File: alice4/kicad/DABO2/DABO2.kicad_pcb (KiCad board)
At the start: 2 copper layers, 96 x 34.1 mm, 61 parts, among them J1 LIPO, J10 THERM, J2 LCD, J3 HOME, J4 +25mA, J5 +25mA, J6 +50mA, J7 5VOUT, J8 PWRSW, J9 5VIN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

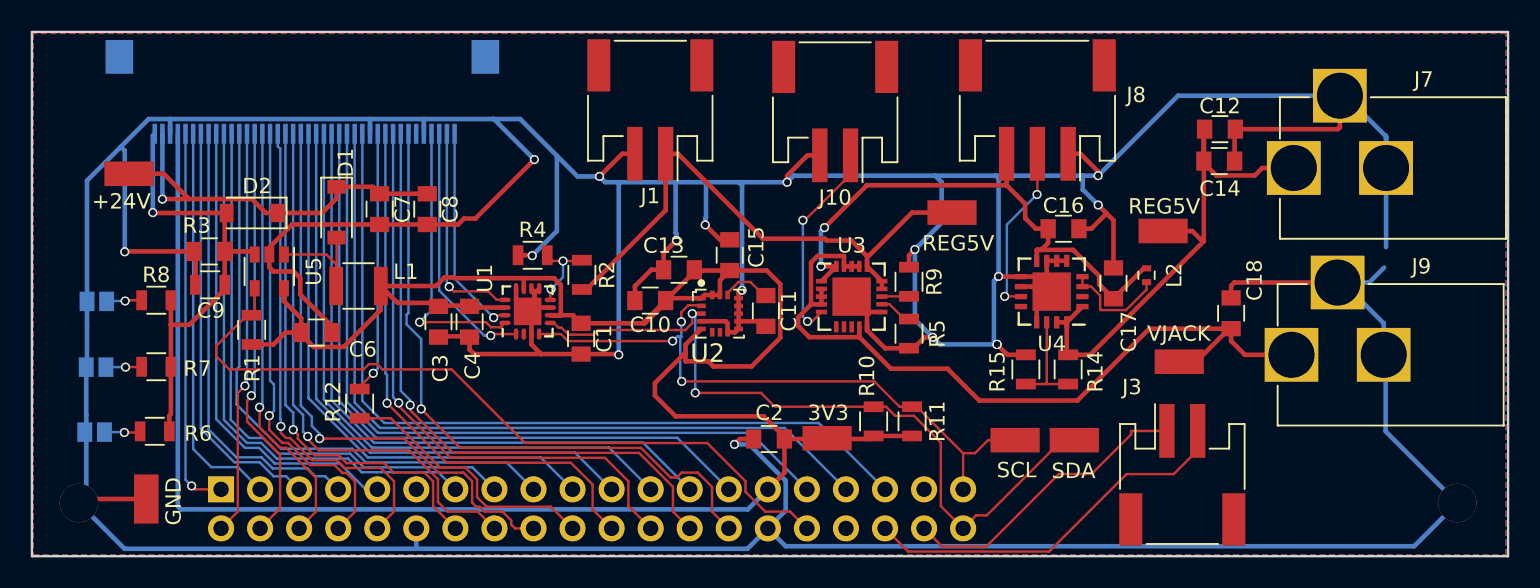
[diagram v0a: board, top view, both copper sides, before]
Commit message: fix holes, add cap for HOME
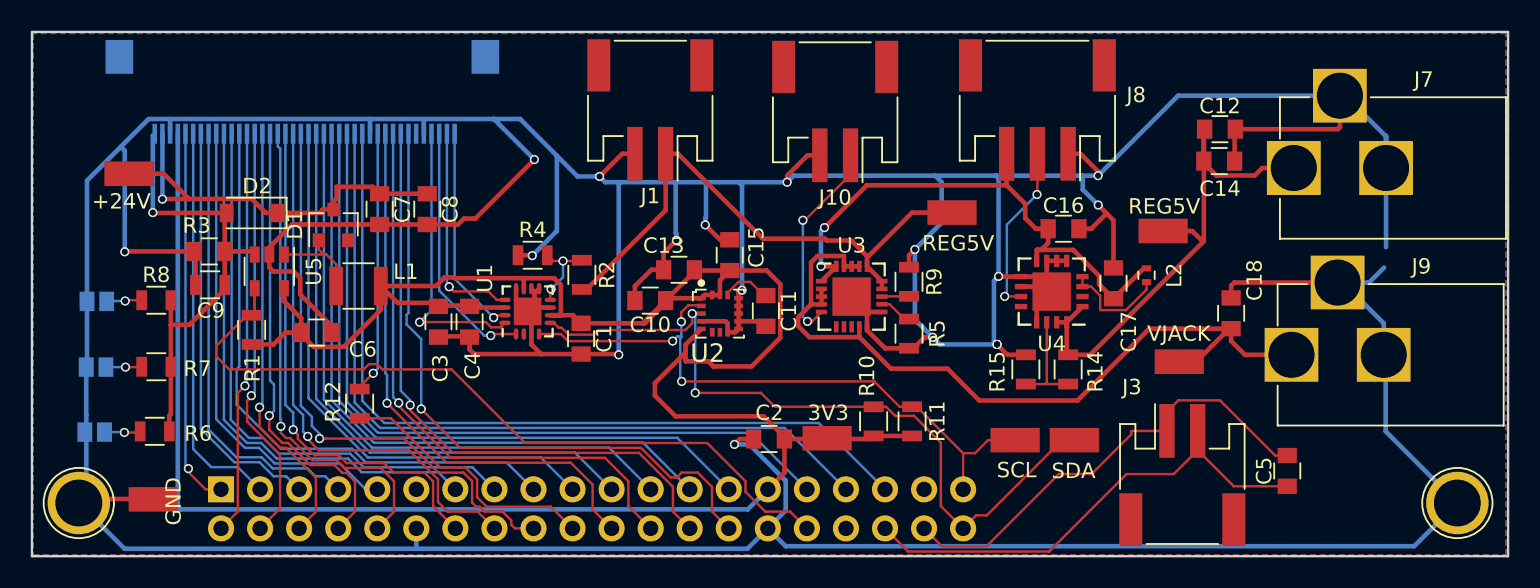
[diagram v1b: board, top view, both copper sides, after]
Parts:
- added C5: .1uF, Capacitors_SMD:C_0805, F.Cu at (186.2, 114.3)
- D1: value MBR0540 -> BAT54; footprint Diodes_SMD:D_SOD-123 -> TO_SOT_Packages_SMD:SOT-23
- HOLE0, HOLE1: footprint Mounting_Holes:MountingHole_2-5mm -> Connect:1pin
- moved D1 0.85 mm to (124.2, 98.3), turned to 90 degrees
- moved TP1 0.45 mm to (112.5, 116.1), turned to 180 degrees
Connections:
- D1 pad 1: LED-A -> Net-(D1-Pad1)
- L1 pad 2: Net-(D1-Pad2) -> Net-(D1-Pad1)
- U5 pad 1: Net-(D1-Pad2) -> Net-(D1-Pad1)
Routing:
- net HOME1: track 19.5 -> 30.4 mm
- net Net-(D1-Pad2): track 8.24 -> 0.00 mm
- net HOME0: track 24.9 -> 31.7 mm
- net Net-(D1-Pad1): track 0.00 -> 6.34 mm

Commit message: fix inductor, fix HOME
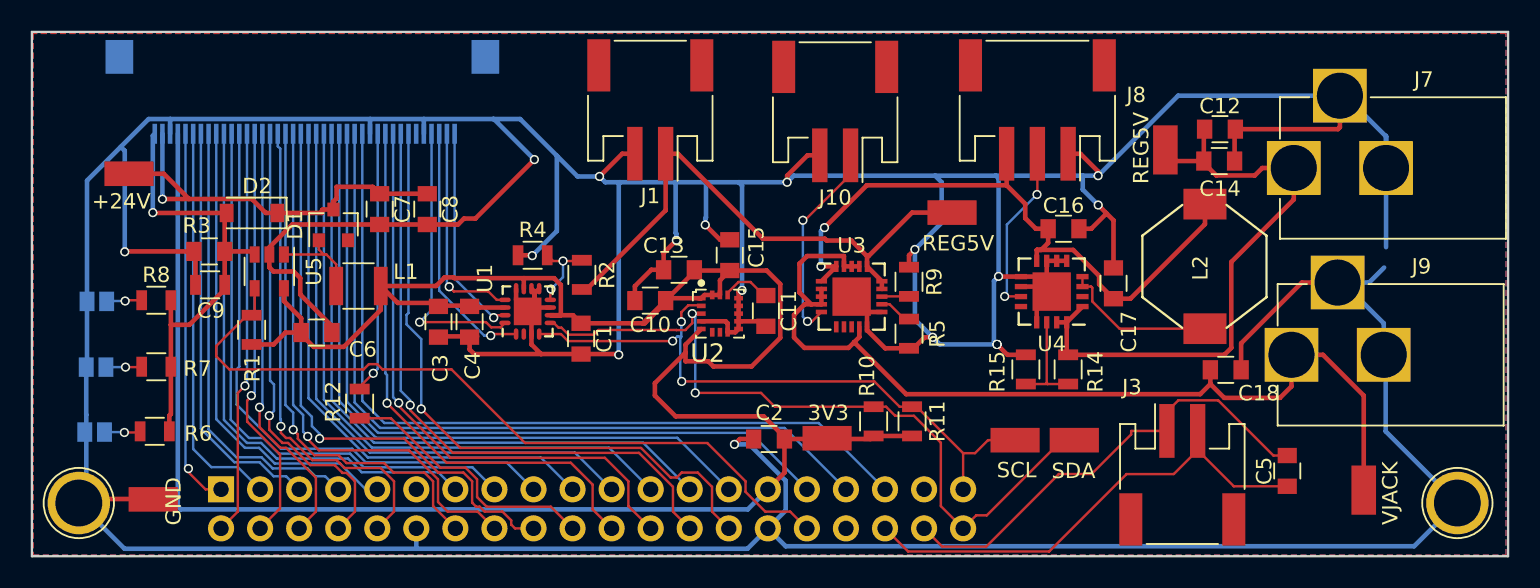
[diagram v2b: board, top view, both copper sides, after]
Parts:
- L2: footprint Inductors_SMD:L_0402 -> inductor_8mm_8mm_smt:inductor_8mm_8mm_smt
- moved TP3 14.6 mm to (191.2, 115.5), turned to 270 degrees
- moved TP6 5.28 mm to (178.3, 93.4), turned to 90 degrees
- moved L2 3.84 mm to (180.9, 101.0)
- moved C18 3.69 mm to (182.2, 107.7), turned to 0 degrees
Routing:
- net VJACK: track 52.3 -> 63.5 mm
- net VBAT: track 36.6 -> 42.9 mm
- net REGULATED5V: track 35.2 -> 40.1 mm
- net Net-(L2-Pad2): track 7.00 -> 10.3 mm
- net GND: track 465.8 -> 467.6 mm

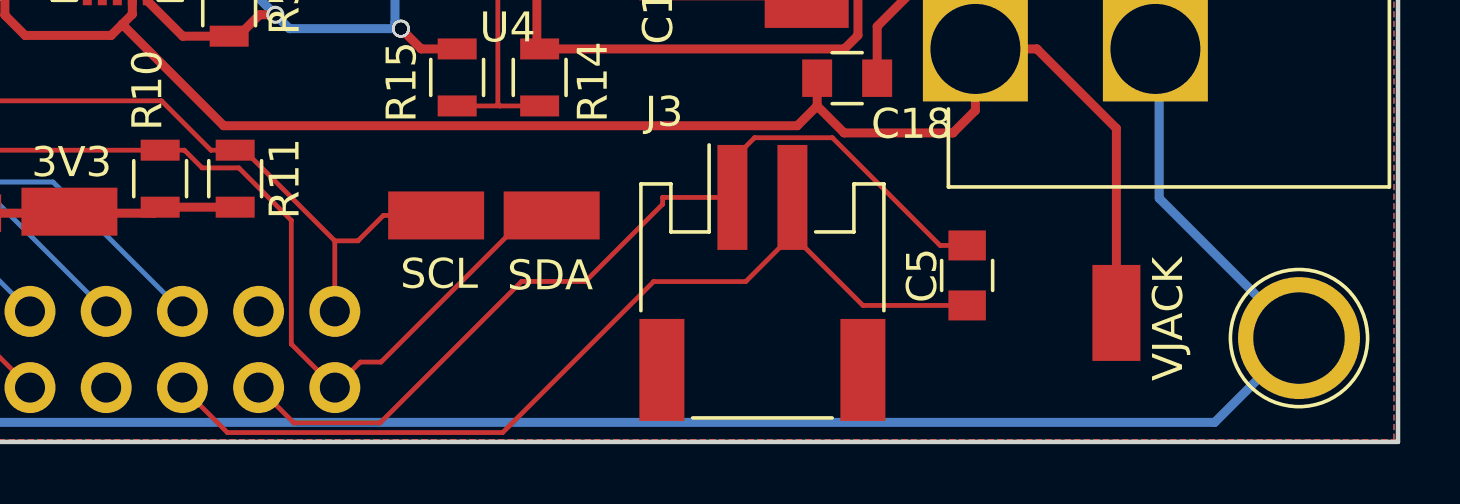
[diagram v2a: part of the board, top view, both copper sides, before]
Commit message: fix inductor, fix HOME
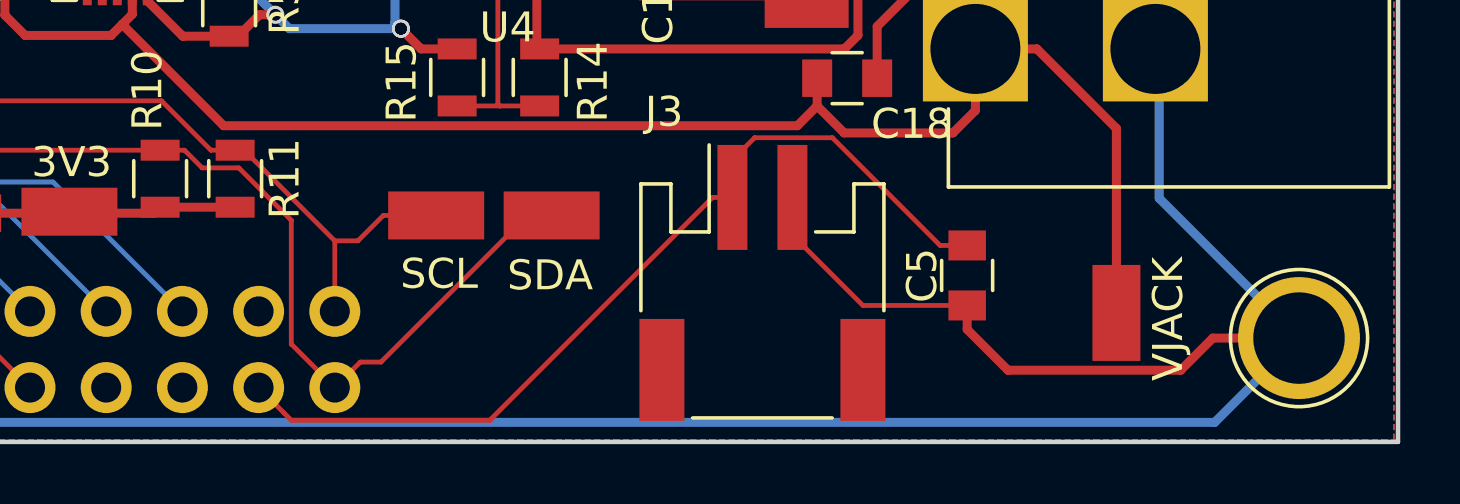
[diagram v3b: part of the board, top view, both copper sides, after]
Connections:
- net HOME1 renamed HOME
- C5 pad 1: HOME0 -> GND
- J3 pad 2: HOME0 -> GND
- P3 pad 36: HOME0 -> Net-(P3-Pad36)
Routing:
- net HOME0: track 31.7 -> 0.00 mm
- net GND: track 467.6 -> 488.6 mm
